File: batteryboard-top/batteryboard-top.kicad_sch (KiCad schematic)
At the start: 6 parts

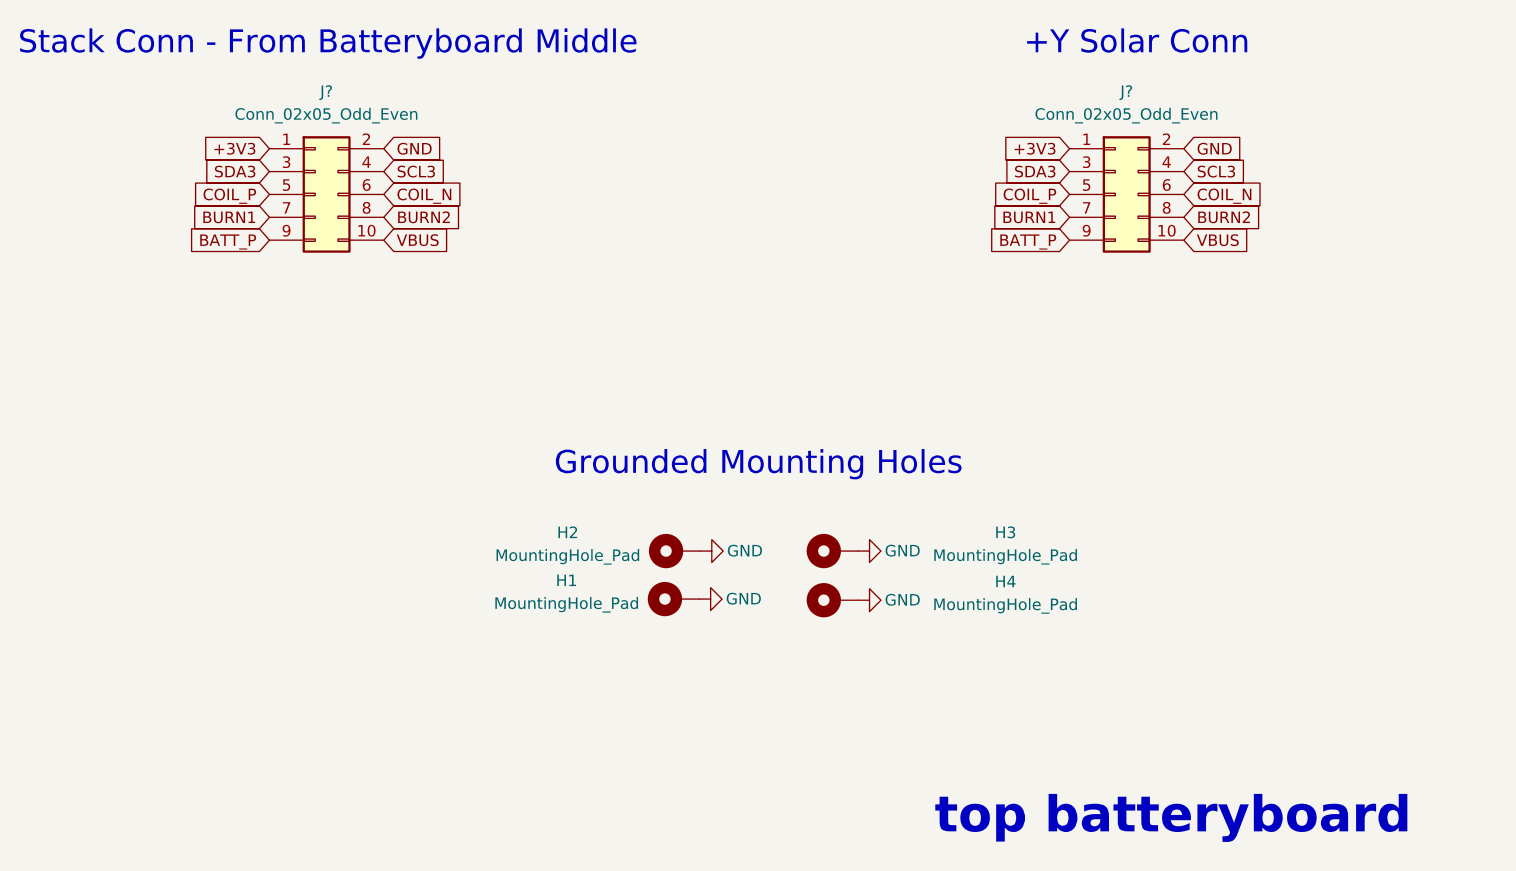
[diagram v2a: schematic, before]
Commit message: remove burn wire signals
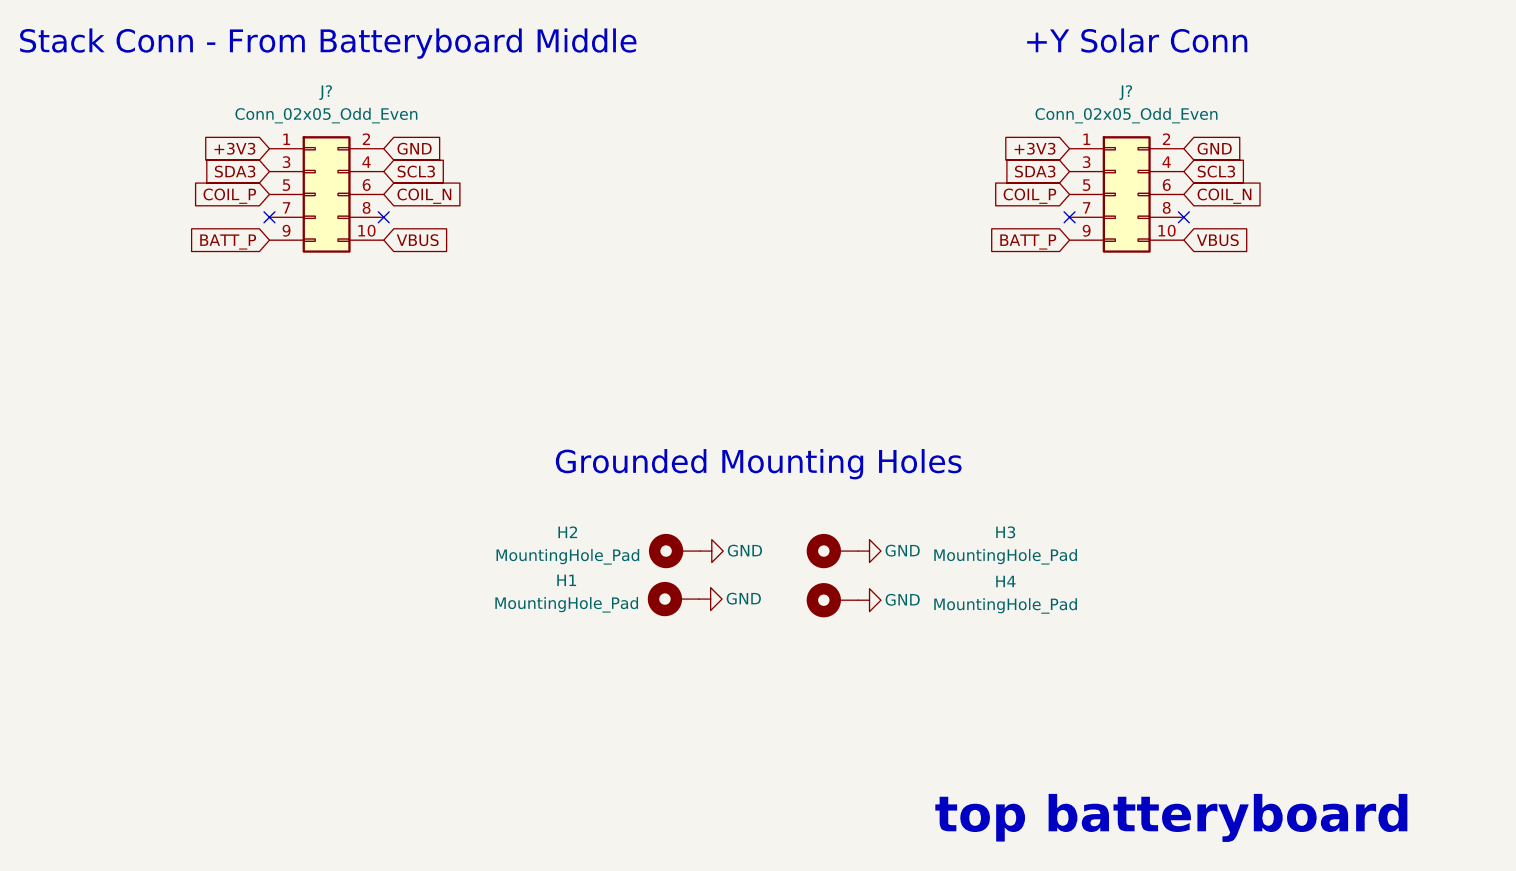
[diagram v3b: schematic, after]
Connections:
- net BURN1: no longer names the net of J?.7 (Pin_7)
- net BURN1: no longer J?.7 (Pin_7)
- net BURN2: no longer names the net of J?.8 (Pin_8)
- net BURN2: no longer J?.8 (Pin_8)
- no-connect marks 0 -> 4
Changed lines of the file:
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@@
     (comment 1 "N. Khera")
   )
+  (no_connect (at 152.4 45.72))
+  (no_connect (at 139.7 45.72))
+  (no_connect (at 63.5 45.72))
+  (no_connect (at 50.8 45.72))
   (text "+Y Solar Conn" (at 134.62 27.94 0)
     (effects (font (size 2.54 2.54)) (justify left bottom))
@@
     )
   )
-  (global_label "BURN1" (shape input) (at 139.7 45.72 180) (fields_autoplaced)
-    (effects (font (size 1.27 1.27)) (justify right))
-    (property "Intersheet References" "${INTERSHEET_REFS}" (id 0) (at 130.8764 45.6406 0)
-      (effects (font (size 1.27 1.27)) (justify right) hide)
-    )
-  )
-  (global_label "BURN2" (shape input) (at 152.4 45.72 0) (fields_autoplaced)
-    (effects (font (size 1.27 1.27)) (justify left))
-    (property "Intersheet References" "${INTERSHEET_REFS}" (id 0) (at 161.2236 45.6406 0)
-      (effects (font (size 1.27 1.27)) (justify left) hide)
-    )
-  )
   (global_label "SCL3" (shape input) (at 152.4 40.64 0) (fields_autoplaced)
     (effects (font (size 1.27 1.27)) (justify left))
@@
     (effects (font (size 1.27 1.27)) (justify left))
     (property "Intersheet References" "${INTERSHEET_REFS}" (id 0) (at 161.3445 43.1006 0)
-      (effects (font (size 1.27 1.27)) (justify left) hide)
-    )
-  )
-  (global_label "BURN2" (shape input) (at 63.5 45.72 0) (fields_autoplaced)
-    (effects (font (size 1.27 1.27)) (justify left))
-    (property "Intersheet References" "${INTERSHEET_REFS}" (id 0) (at 72.3236 45.6406 0)
       (effects (font (size 1.27 1.27)) (justify left) hide)
     )
@@
       (effects (font (size 1.27 1.27)) (justify right) hide)
     )
-  )
-  (global_label "BURN1" (shape input) (at 50.8 45.72 180) (fields_autoplaced)
-    (effects (font (size 1.27 1.27)) (justify right))
-    (property "Intersheet References" "${INTERSHEET_REFS}" (id 0) (at 41.9764 45.6406 0)
-      (effects (font (size 1.27 1.27)) (justify right) hide)
-    )

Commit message: NC on pins 1 and 2 to match with -Y
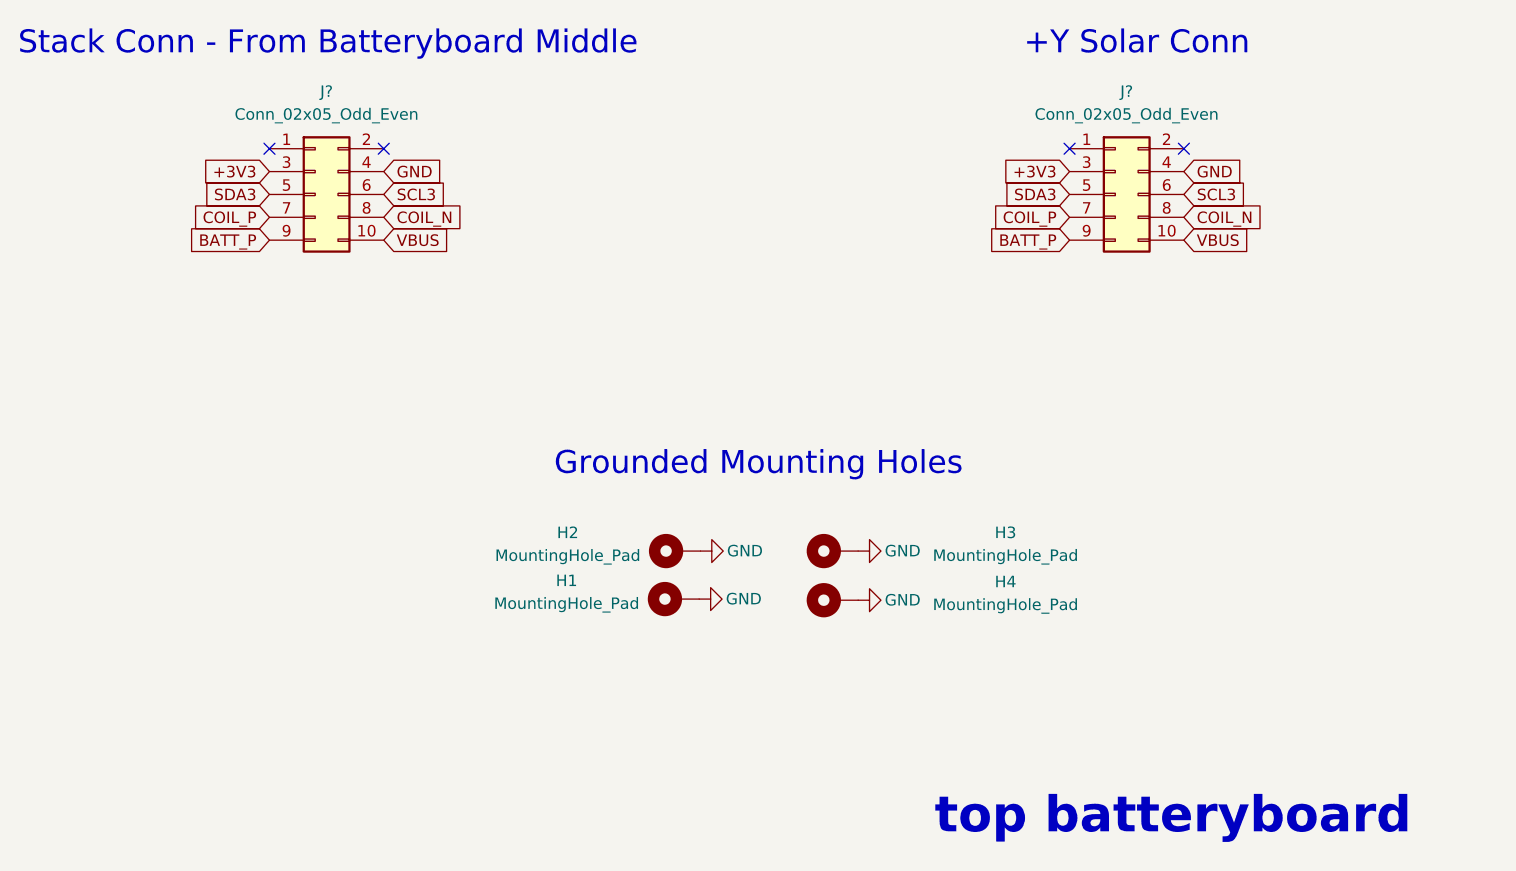
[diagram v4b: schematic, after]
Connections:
- net +3V3: now also J?.3 (Pin_3), J?.3 (Pin_3); no longer J?.1 (Pin_1), J?.1 (Pin_1)
- net COIL_N: now also J?.8 (Pin_8), J?.8 (Pin_8); no longer J?.6 (Pin_6), J?.6 (Pin_6)
- net COIL_P: now also J?.7 (Pin_7), J?.7 (Pin_7); no longer J?.5 (Pin_5), J?.5 (Pin_5)
- net GND: now also J?.4 (Pin_4), J?.4 (Pin_4); no longer J?.2 (Pin_2), J?.2 (Pin_2)
- net SCL3: now also J?.6 (Pin_6), J?.6 (Pin_6); no longer J?.4 (Pin_4), J?.4 (Pin_4)
- net SDA3: now also J?.5 (Pin_5), J?.5 (Pin_5); no longer J?.3 (Pin_3), J?.3 (Pin_3)
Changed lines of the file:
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@@
     (comment 1 "N. Khera")
   )
-  (no_connect (at 152.4 45.72))
-  (no_connect (at 139.7 45.72))
-  (no_connect (at 63.5 45.72))
-  (no_connect (at 50.8 45.72))
+  (no_connect (at 152.4 38.1))
+  (no_connect (at 139.7 38.1))
+  (no_connect (at 63.5 38.1))
+  (no_connect (at 50.8 38.1))
   (text "+Y Solar Conn" (at 134.62 27.94 0)
     (effects (font (size 2.54 2.54)) (justify left bottom))
@@
     (effects (font (size 3.9878 3.9878) (thickness 1.016) bold) (justify left bottom))
   )
-  (global_label "COIL_P" (shape input) (at 139.7 43.18 180) (fields_autoplaced)
+  (global_label "COIL_P" (shape input) (at 139.7 45.72 180) (fields_autoplaced)
     (effects (font (size 1.27 1.27)) (justify right))
-    (property "Intersheet References" "${INTERSHEET_REFS}" (id 0) (at 130.8159 43.1006 0)
+    (property "Intersheet References" "${INTERSHEET_REFS}" (id 0) (at 130.8159 45.6406 0)
       (effects (font (size 1.27 1.27)) (justify right) hide)
     )
   )
-  (global_label "COIL_N" (shape input) (at 63.5 43.18 0) (fields_autoplaced)
+  (global_label "COIL_N" (shape input) (at 63.5 45.72 0) (fields_autoplaced)
     (effects (font (size 1.27 1.27)) (justify left))
-    (property "Intersheet References" "${INTERSHEET_REFS}" (id 0) (at 72.4445 43.1006 0)
+    (property "Intersheet References" "${INTERSHEET_REFS}" (id 0) (at 72.4445 45.6406 0)
       (effects (font (size 1.27 1.27)) (justify left) hide)
     )
   )
-  (global_label "GND" (shape input) (at 152.4 38.1 0) (fields_autoplaced)
+  (global_label "GND" (shape input) (at 152.4 40.64 0) (fields_autoplaced)
     (effects (font (size 1.27 1.27)) (justify left))
-    (property "Intersheet References" "${INTERSHEET_REFS}" (id 0) (at 158.6836 38.0206 0)
+    (property "Intersheet References" "${INTERSHEET_REFS}" (id 0) (at 158.6836 40.5606 0)
       (effects (font (size 1.27 1.27)) (justify left) hide)
     )
   )
-  (global_label "GND" (shape input) (at 63.5 38.1 0) (fields_autoplaced)
+  (global_label "GND" (shape input) (at 63.5 40.64 0) (fields_autoplaced)
     (effects (font (size 1.27 1.27)) (justify left))
-    (property "Intersheet References" "${INTERSHEET_REFS}" (id 0) (at 69.7836 38.0206 0)
+    (property "Intersheet References" "${INTERSHEET_REFS}" (id 0) (at 69.7836 40.5606 0)
       (effects (font (size 1.27 1.27)) (justify left) hide)
     )
@@
     )
   )
-  (global_label "SCL3" (shape input) (at 63.5 40.64 0) (fields_autoplaced)
+  (global_label "SCL3" (shape input) (at 63.5 43.18 0) (fields_autoplaced)
     (effects (font (size 1.27 1.27)) (justify left))
-    (property "Intersheet References" "${INTERSHEET_REFS}" (id 0) (at 70.6302 40.5606 0)
+    (property "Intersheet References" "${INTERSHEET_REFS}" (id 0) (at 70.6302 43.1006 0)
       (effects (font (size 1.27 1.27)) (justify left) hide)
     )
   )
-  (global_label "SCL3" (shape input) (at 152.4 40.64 0) (fields_autoplaced)
+  (global_label "SCL3" (shape input) (at 152.4 43.18 0) (fields_autoplaced)
     (effects (font (size 1.27 1.27)) (justify left))
-    (property "Intersheet References" "${INTERSHEET_REFS}" (id 0) (at 159.5302 40.5606 0)
+    (property "Intersheet References" "${INTERSHEET_REFS}" (id 0) (at 159.5302 43.1006 0)
       (effects (font (size 1.27 1.27)) (justify left) hide)
     )
   )
-  (global_label "COIL_N" (shape input) (at 152.4 43.18 0) (fields_autoplaced)
+  (global_label "COIL_N" (shape input) (at 152.4 45.72 0) (fields_autoplaced)
     (effects (font (size 1.27 1.27)) (justify left))
-    (property "Intersheet References" "${INTERSHEET_REFS}" (id 0) (at 161.3445 43.1006 0)
+    (property "Intersheet References" "${INTERSHEET_REFS}" (id 0) (at 161.3445 45.6406 0)
       (effects (font (size 1.27 1.27)) (justify left) hide)
     )
   )
-  (global_label "+3V3" (shape input) (at 50.8 38.1 180) (fields_autoplaced)
+  (global_label "+3V3" (shape input) (at 50.8 40.64 180) (fields_autoplaced)
     (effects (font (size 1.27 1.27)) (justify right))
-    (property "Intersheet References" "${INTERSHEET_REFS}" (id 0) (at 43.3069 38.0206 0)
+    (property "Intersheet References" "${INTERSHEET_REFS}" (id 0) (at 43.3069 40.5606 0)
       (effects (font (size 1.27 1.27)) (justify right) hide)
     )
   )
-  (global_label "+3V3" (shape input) (at 139.7 38.1 180) (fields_autoplaced)
+  (global_label "+3V3" (shape input) (at 139.7 40.64 180) (fields_autoplaced)
     (effects (font (size 1.27 1.27)) (justify right))
-    (property "Intersheet References" "${INTERSHEET_REFS}" (id 0) (at 132.2069 38.0206 0)
+    (property "Intersheet References" "${INTERSHEET_REFS}" (id 0) (at 132.2069 40.5606 0)
       (effects (font (size 1.27 1.27)) (justify right) hide)
     )
   )
-  (global_label "SDA3" (shape input) (at 139.7 40.64 180) (fields_autoplaced)
+  (global_label "SDA3" (shape input) (at 139.7 43.18 180) (fields_autoplaced)
     (effects (font (size 1.27 1.27)) (justify right))
-    (property "Intersheet References" "${INTERSHEET_REFS}" (id 0) (at 132.5093 40.5606 0)
+    (property "Intersheet References" "${INTERSHEET_REFS}" (id 0) (at 132.5093 43.1006 0)
       (effects (font (size 1.27 1.27)) (justify right) hide)
     )
   )
-  (global_label "SDA3" (shape input) (at 50.8 40.64 180) (fields_autoplaced)
+  (global_label "SDA3" (shape input) (at 50.8 43.18 180) (fields_autoplaced)
     (effects (font (size 1.27 1.27)) (justify right))
-    (property "Intersheet References" "${INTERSHEET_REFS}" (id 0) (at 43.6093 40.5606 0)
+    (property "Intersheet References" "${INTERSHEET_REFS}" (id 0) (at 43.6093 43.1006 0)
       (effects (font (size 1.27 1.27)) (justify right) hide)
     )
@@
     )
   )
-  (global_label "COIL_P" (shape input) (at 50.8 43.18 180) (fields_autoplaced)
+  (global_label "COIL_P" (shape input) (at 50.8 45.72 180) (fields_autoplaced)
     (effects (font (size 1.27 1.27)) (justify right))
-    (property "Intersheet References" "${INTERSHEET_REFS}" (id 0) (at 41.9159 43.1006 0)
+    (property "Intersheet References" "${INTERSHEET_REFS}" (id 0) (at 41.9159 45.6406 0)
       (effects (font (size 1.27 1.27)) (justify right) hide)
     )
